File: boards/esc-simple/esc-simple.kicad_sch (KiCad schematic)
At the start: 4 parts, among them J101 XT60PW-M, U101 MIC4604YM

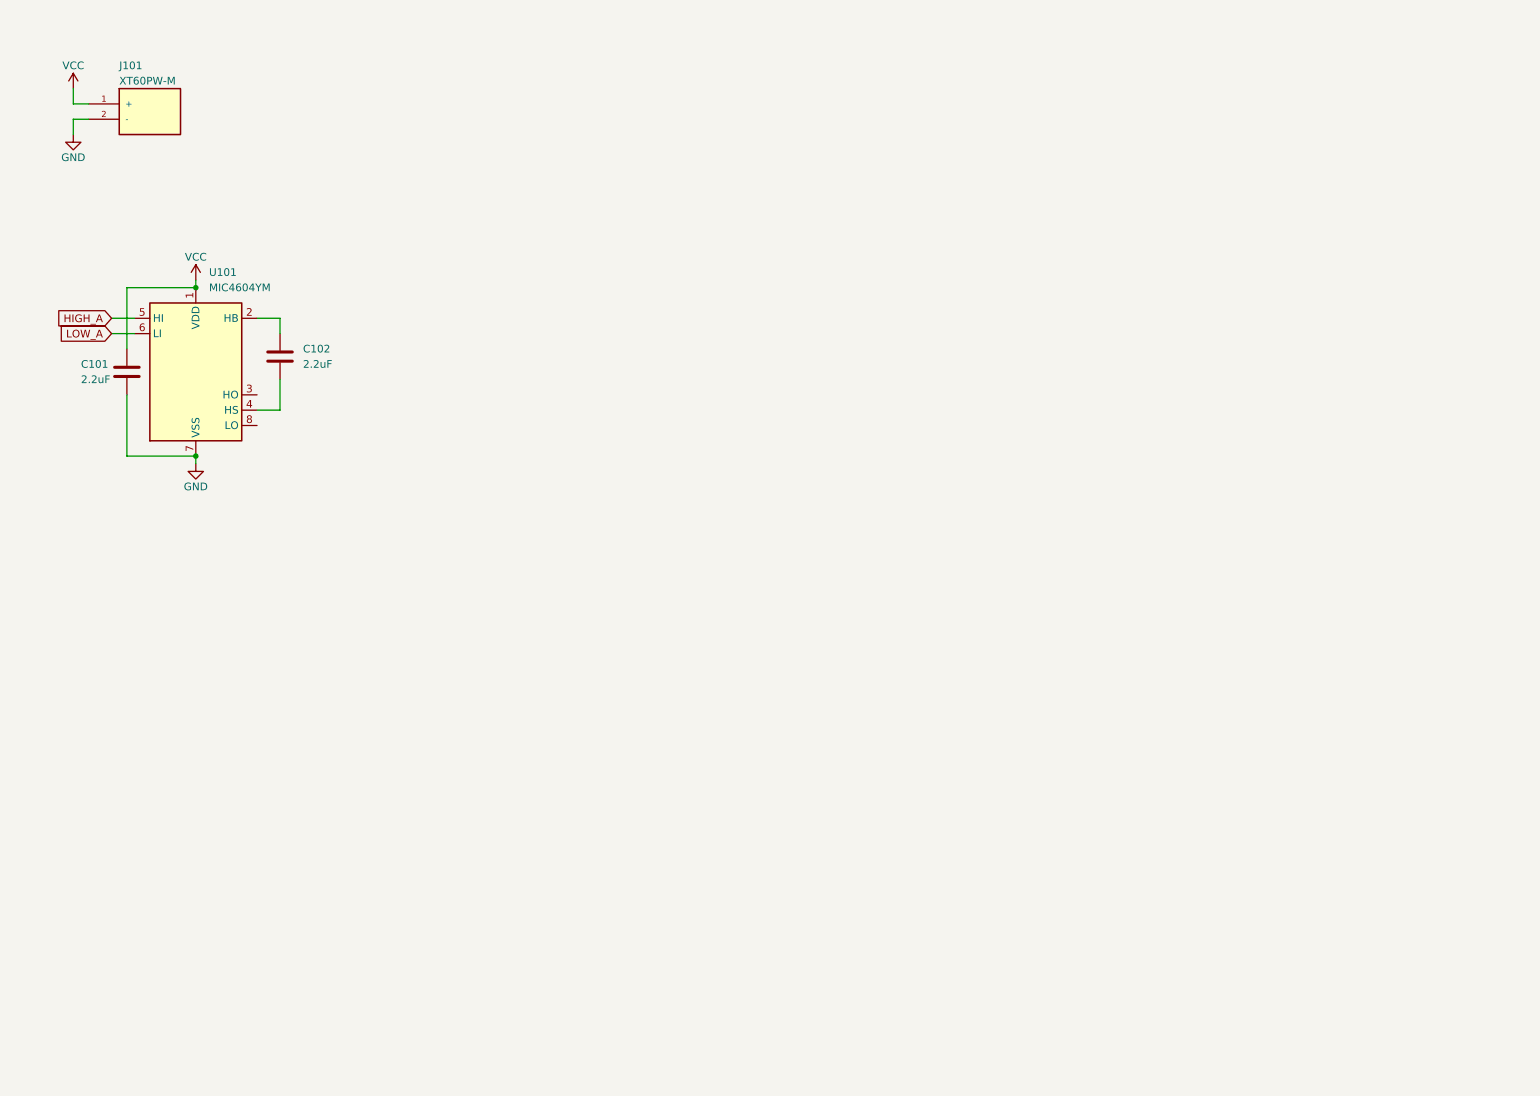
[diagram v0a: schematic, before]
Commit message: added MIC4606 and IRFR mosfet
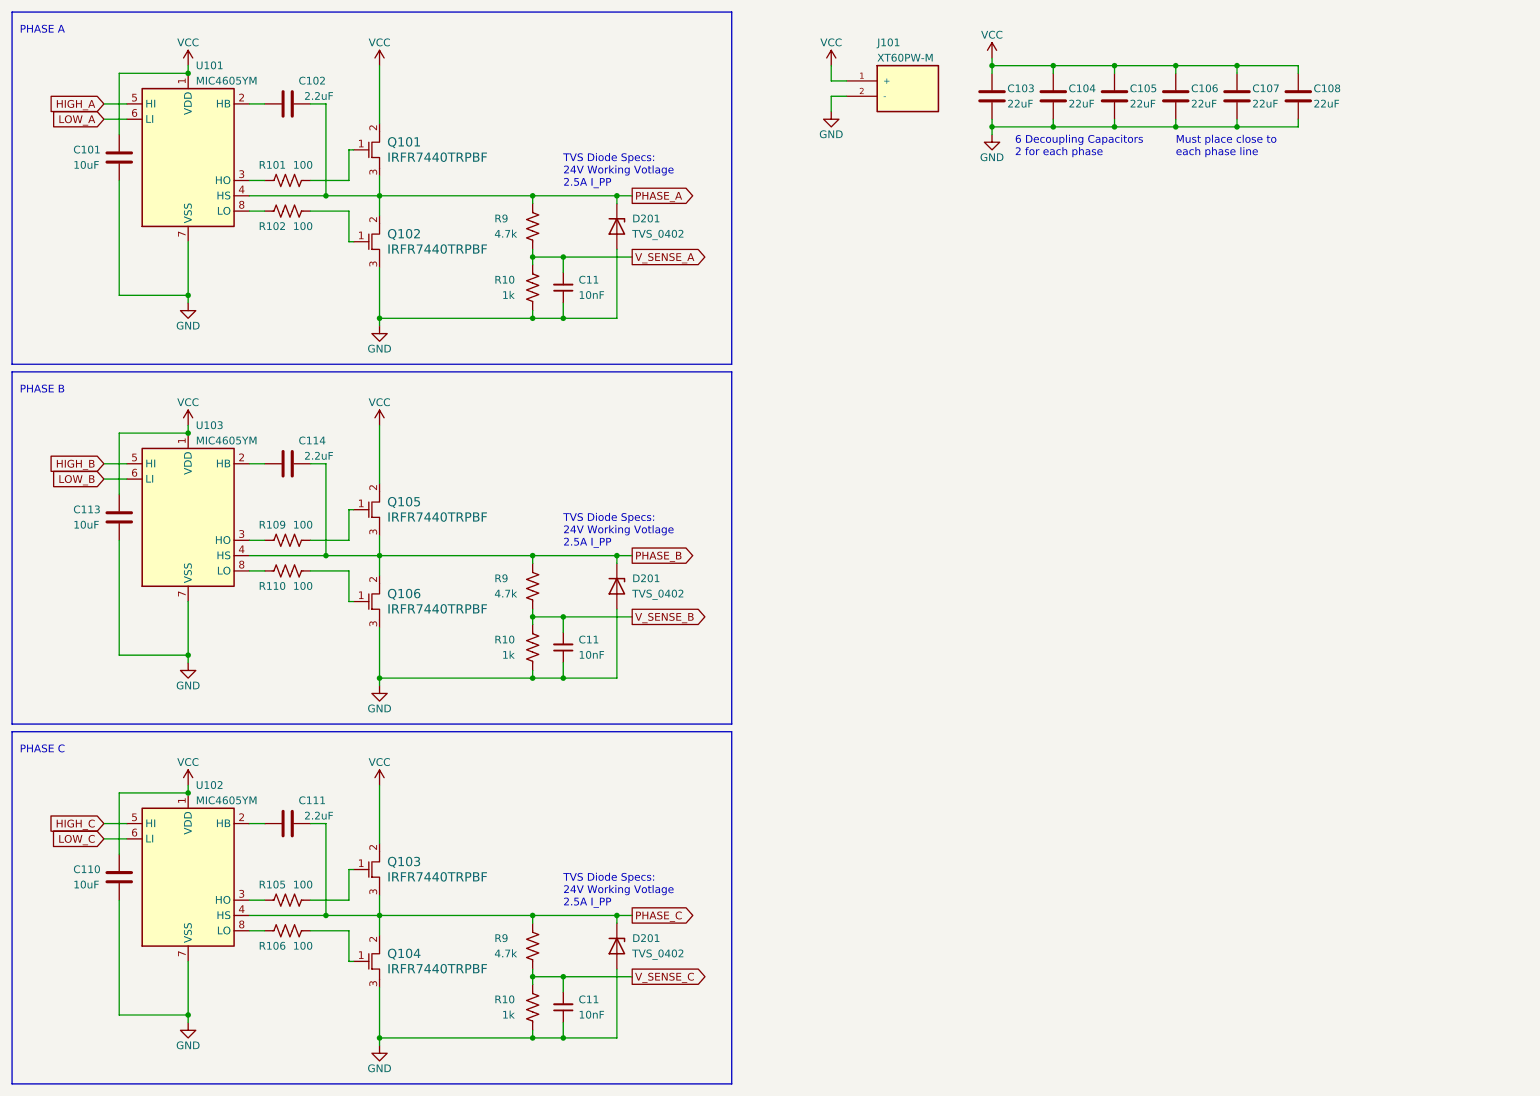
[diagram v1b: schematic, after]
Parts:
- added C103, C104, C105, C106, C107, C108: 22uF, Capacitor_SMD:C_1210_3225Metric, symbol Device:C
- added C11 (x3): 10nF, Capacitor_SMD:C_0603_1608Metric, symbol Device:C_Small
- added C110, C113: 10uF, Capacitor_SMD:C_0603_1608Metric, symbol Device:C
- added C111, C114: 2.2uF, Capacitor_SMD:C_0603_1608Metric, symbol Device:C
- added D201 (x3): TVS_0402, Diode_SMD:D_01005_0402Metric, symbol Device:D_Zener
- added Q101, Q102, Q103, Q104, Q105, Q106: IRFR7440TRPBF, D-Pak_IRFR7440TRPBF_INF, symbol IRF7440TRPBF:IRFR7440TRPBF
- added R10 (x3): 1k, Resistor_SMD:R_0603_1608Metric, symbol Device:R_US
- added R101, R102, R105, R106, R109, R110: 100, Resistor_SMD:R_0603_1608Metric, symbol Device:R_US
- added R9 (x3): 4.7k, Resistor_SMD:R_0603_1608Metric, symbol Device:R_US
- added U102, U103: MIC4605YM, Package_SO:SOIC-8_3.9x4.9mm_P1.27mm, symbol Driver_FET:MIC4604YM
- C101: value 2.2uF -> 10uF
- U101: value MIC4604YM -> MIC4605YM
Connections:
- net GND: now also C103.2, C104.2, C105.2, C106.2, C107.2, C108.2, C11.1, C11.1, C11.1, C110.2, C113.2, D201.2 (A), D201.2 (A), D201.2 (A), Q102.3 (D), Q104.3 (D), Q106.3 (D), R10.2, R10.2, R10.2, U102.7 (VSS), U103.7 (VSS)
- net VCC: now also C103.1, C104.1, C105.1, C106.1, C107.1, C108.1, C110.1, C113.1, Q101.2 (S), Q103.2 (S), Q105.2 (S), U102.1 (VDD), U103.1 (VDD)
- net at U101.3 (HO): now also R101.2
- net PHASE_A: now reaches C102.2, U101.4 (HS)
- net PHASE_A: now also D201.1 (K), Q101.3 (D), Q102.2 (S), R9.1
- net at U101.8 (LO): now also R102.2
- new net: Q104.1 (G), R106.1
- new net: R106.2, U102.8 (LO)
- new net: Q105.1 (G), R109.1
- new net: R109.2, U103.3 (HO)
- new net: C114.1, U103.2 (HB)
- new net: R110.2, U103.8 (LO)
- new net: C111.1, U102.2 (HB)
- new net: R105.2, U102.3 (HO)
- new net: Q101.1 (G), R101.1
- new net: Q103.1 (G), R105.1
- new net: Q102.1 (G), R102.1
- new net: Q106.1 (G), R110.1
- new net HIGH_B: U103.5 (HI)
- new net HIGH_C: U102.5 (HI)
- new net LOW_B: U103.6 (LI)
- new net LOW_C: U102.6 (LI)
- new net PHASE_B: C114.2, D201.1 (K), Q105.3 (D), Q106.2 (S), R9.1, U103.4 (HS)
- new net PHASE_C: C111.2, D201.1 (K), Q103.3 (D), Q104.2 (S), R9.1, U102.4 (HS)
- new net V_SENSE_A: C11.2, R10.1, R9.2
- new net V_SENSE_B: C11.2, R10.1, R9.2
- new net V_SENSE_C: C11.2, R10.1, R9.2
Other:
- note added: "6 Decoupling Capacitors 2 for each phase"
- note added: "Must place close to each phase line"
- note added: "PHASE A"
- note added: "PHASE B"
- note added: "PHASE C"
- note added: "TVS Diode Specs: 24V Working Votlage 2.5A I_PP"
- moved on the sheet: C101, C102, J101, U101

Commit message: finished esc simple schematic
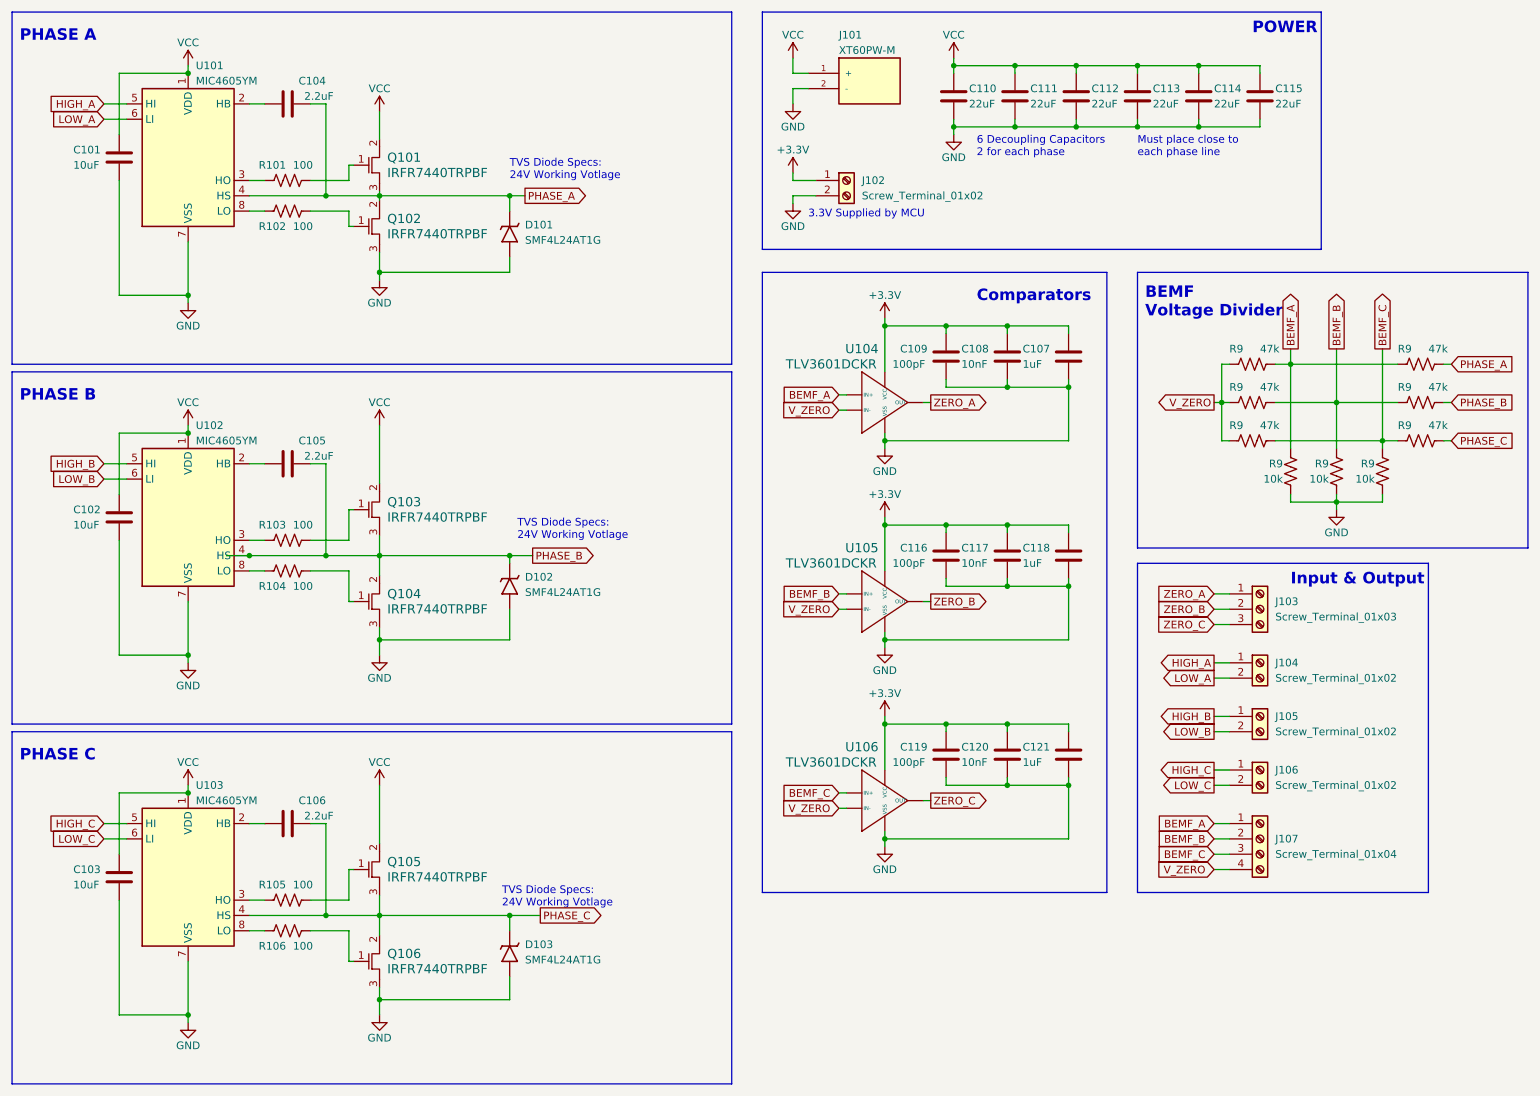
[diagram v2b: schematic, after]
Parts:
- removed C11 (x3): 10nF, Capacitor_SMD:C_0603_1608Metric, symbol Device:C_Small
- removed D201 (x3): TVS_0402, Diode_SMD:D_01005_0402Metric, symbol Device:D_Zener
- removed R10 (x3): 1k, Resistor_SMD:R_0603_1608Metric, symbol Device:R_US
- removed R9 (x3): 4.7k, Resistor_SMD:R_0603_1608Metric, symbol Device:R_US
- added C107, C118, C121: 1uF, Capacitor_SMD:C_0603_1608Metric, symbol Device:C
- added C108, C117, C120: 10nF, Capacitor_SMD:C_0603_1608Metric, symbol Device:C
- added C109, C116, C119: 100pF, Capacitor_SMD:C_0603_1608Metric, symbol Device:C
- added D101, D102, D103: SMF4L24AT1G, SODFL3619X98N, symbol SMF4L24AT1G:SMF4L24AT1G
- added J102, J104, J105, J106: Screw_Terminal_01x02, TerminalBlock_Phoenix:TerminalBlock_Phoenix_PT-1,5-2-3.5-H_1x02_P3.50mm_Horizontal, symbol Connector:Screw_Terminal_01x02
- added J103: Screw_Terminal_01x03, symbol Connector:Screw_Terminal_01x03
- added J107: Screw_Terminal_01x04, TerminalBlock_Phoenix:TerminalBlock_Phoenix_PT-1,5-4-3.5-H_1x04_P3.50mm_Horizontal, symbol Connector:Screw_Terminal_01x04
- added R9 (x3): 10k, Resistor_SMD:R_0603_1608Metric, symbol Device:R_US
- added R9 (x6): 47k, Resistor_SMD:R_0603_1608Metric, symbol Device:R_US
- added U104, U105, U106: TLV3601DCKR, SC_601DCKT_TEX, symbol TLV3601DCKR:TLV3601DCKR
- renumbered C113 to C102, C110 to C103, C102 to C104, C114 to C105, C111 to C106, C103 to C110, C104 to C111, C105 to C112, C106 to C113, C107 to C114, C108 to C115, Q105 to Q103, Q106 to Q104, Q103 to Q105, Q104 to Q106, R109 to R103, R110 to R104, U103 to U102, U102 to U103
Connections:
- net GND: now also C107.2, C108.2, C109.2, C116.2, C117.2, C118.2, C119.2, C120.2, C121.2, D101.2 (A), D102.2 (A), D103.2 (A), J102.2 (Pin_2), R9.1, R9.1, R9.1, U104.2 (VSS), U105.2 (VSS), U106.2 (VSS)
- net HIGH_A: now also J104.1 (Pin_1)
- net HIGH_B: now also J105.1 (Pin_1)
- net HIGH_C: now also J106.1 (Pin_1)
- net LOW_A: now also J104.2 (Pin_2)
- net LOW_B: now also J105.2 (Pin_2)
- net LOW_C: now also J106.2 (Pin_2)
- net PHASE_A: now also D101.1 (K), R9.1
- net PHASE_B: now also D102.1 (K), R9.1
- net PHASE_C: now also D103.1 (K), R9.1
- new net +3.3V: C107.1, C108.1, C109.1, C116.1, C117.1, C118.1, C119.1, C120.1, C121.1, J102.1 (Pin_1), U104.5 (VCC), U105.5 (VCC), U106.5 (VCC)
- new net BEMF_A: J107.1 (Pin_1), R9.1, R9.2, R9.2, U104.3 (IN+)
- new net BEMF_B: J107.2 (Pin_2), R9.1, R9.2, R9.2, U105.3 (IN+)
- new net BEMF_C: J107.3 (Pin_3), R9.1, R9.2, R9.2, U106.3 (IN+)
- new net V_ZERO: J107.4 (Pin_4), R9.2, R9.2, R9.2, U104.4 (IN-), U105.4 (IN-), U106.4 (IN-)
- new net ZERO_A: J103.1 (Pin_1), U104.1 (OUT)
- new net ZERO_B: J103.2 (Pin_2), U105.1 (OUT)
- new net ZERO_C: J103.3 (Pin_3), U106.1 (OUT)
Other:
- note added: "3.3V Supplied by MCU"
- note added: "BEMF Voltage Divider"
- note added: "Comparators"
- note added: "Input & Output"
- note added: "POWER"
- note added: "TVS Diode Specs: 24V Working Votlage"
- note removed: "TVS Diode Specs: 24V Working Votlage 2.5A I_PP"
- moved on the sheet: C110, C111, C112, C113, C114, C115, J101, Q101, Q102
